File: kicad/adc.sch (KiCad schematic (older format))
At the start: 18 parts, among them U1 SIT1602BI-21-XXE-8.192000G

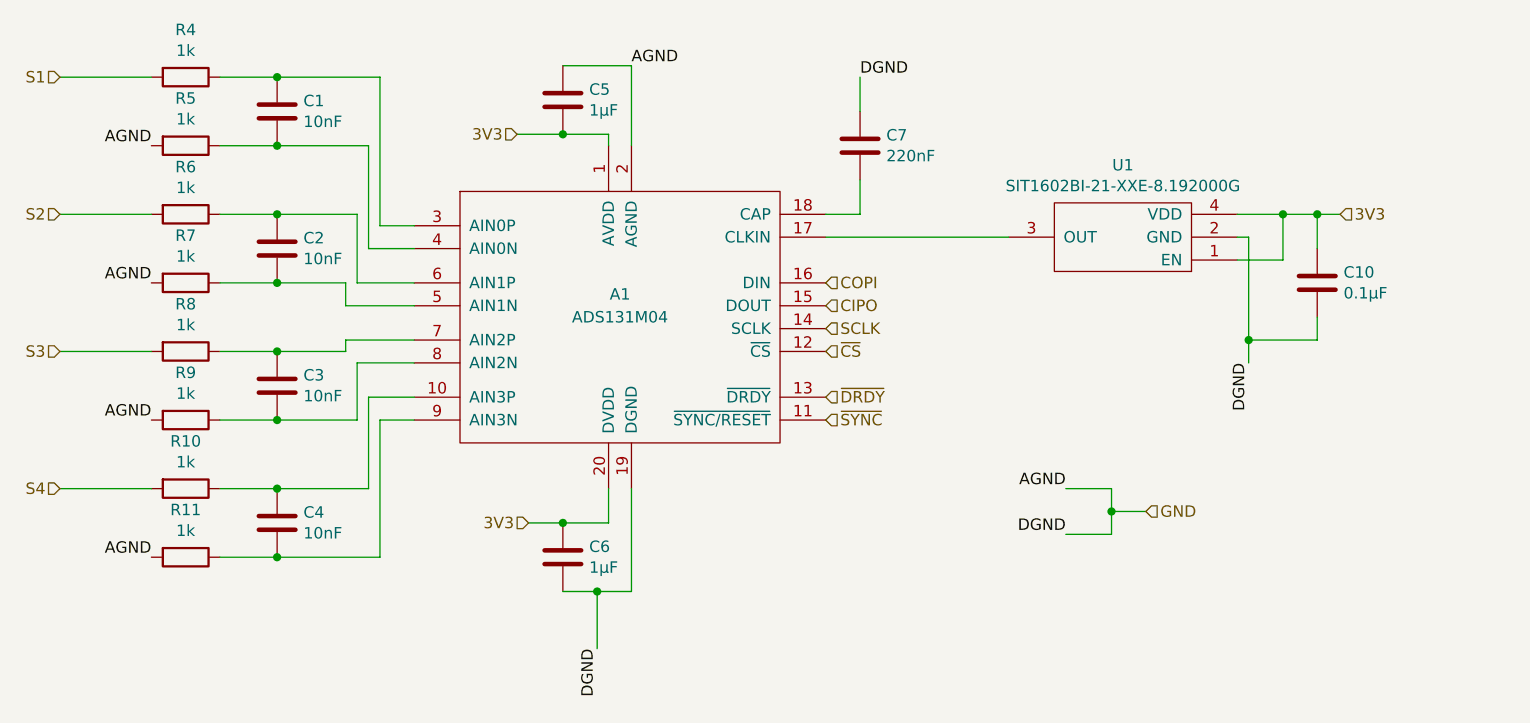
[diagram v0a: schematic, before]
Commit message: switch clock and add bypass
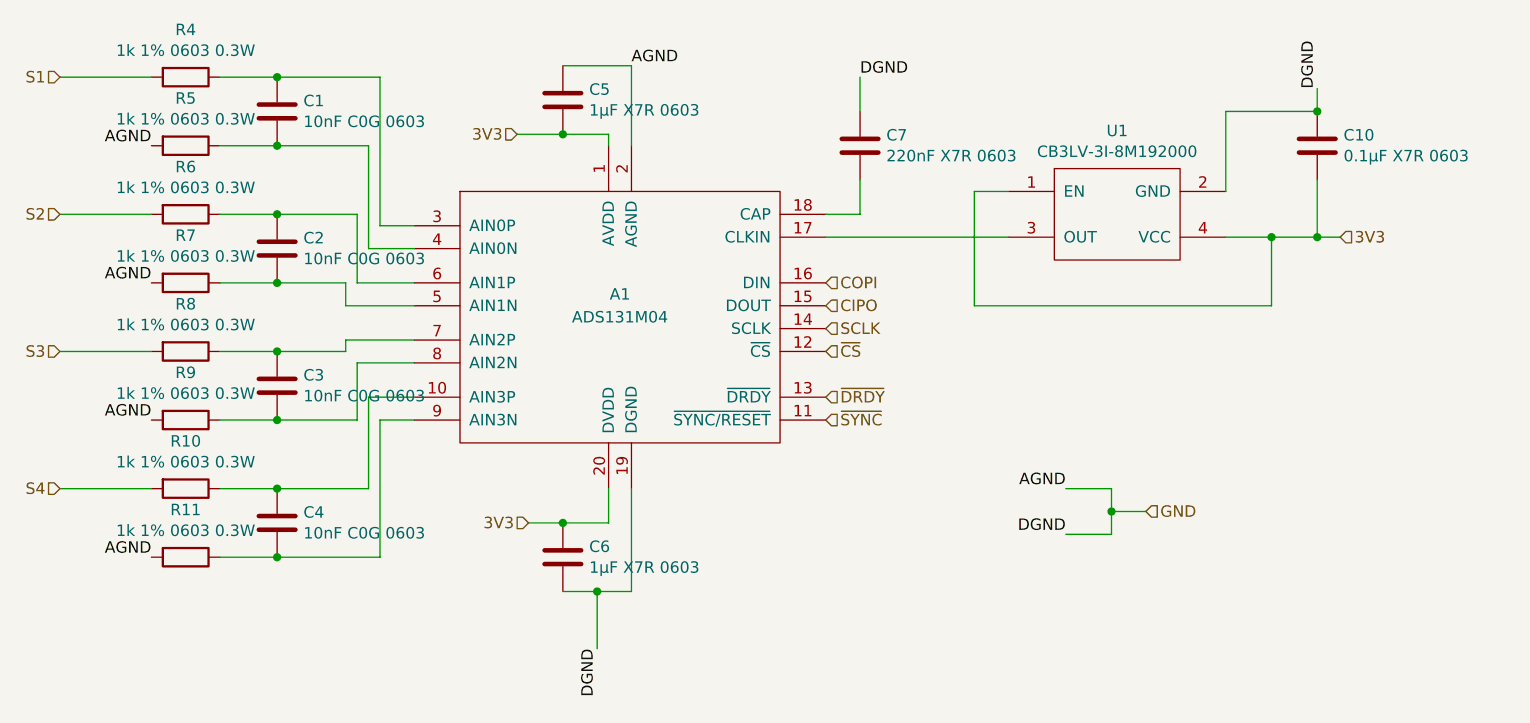
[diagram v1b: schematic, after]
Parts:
- removed U1: SIT1602BI-21-XXE-8.192000G, HH_SiTime:SIT1602BI-21-XXE-8.192000G, symbol HH_SiTime:SIT1602BI-21-XXE-8.192000G
- added U1: CB3LV-3I-8M192000, HH_CTS-FrequencyControls:CB3LV-3I-8M192000, symbol HH_CTS-FrequencyControls:CB3LV-3I-8M192000
- C1, C2, C3, C4: value 10nF -> 10nF C0G 0603
- C10: value 0.1µF -> 0.1µF X7R 0603
- C5, C6: value 1µF -> 1µF X7R 0603
- C7: value 220nF -> 220nF X7R 0603
- R10, R11, R4, R5, R6, R7, R8, R9: value 1k -> 1k 1% 0603 0.3W
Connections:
- net 3V3: now also C10.2, U1.1 (EN), U1.4 (VCC); no longer C10.1
- net GND: now also C10.1, U1.2 (GND); no longer C10.2
- net at A1.17 (CLKIN): now also U1.3 (OUT)
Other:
- moved on the sheet: C10
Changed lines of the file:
@@
 	1    0    0    -1
 $EndComp
-$Comp
-L HH_SiTime:SIT1602BI-21-XXE-8.192000G U?
-U 1 1 5FC7855A
-P 7850 3450
-AR Path="/5FC7855A" Ref="U?"  Part="1"
-AR Path="/5FC723A8/5FC7855A" Ref="U1"  Part="1"
-F 0 "U1" H 7850 3135 50  0000 C CNN
-F 1 "SIT1602BI-21-XXE-8.192000G" H 7850 3226 50  0000 C CNN
-F 2 "HH_SiTime:SIT1602BI-21-XXE-8.192000G" H 7850 3450 50  0001 C CNN
-F 3 "https://www.sitime.com/datasheet/SiT1602" H 7850 3450 50  0001 C CNN
-F 4 "1473-SIT1602BI-21-XXE-8.192000G-ND" H 7850 3450 50  0001 C CNN "Digi-Key Part Number"
-F 5 "SiTime" H 7850 3450 50  0001 C CNN "Manufacturer"
-F 6 "SIT1602BI-21-XXE-8.192000G" H 7850 3450 50  0001 C CNN "Manufacturer Part Number"
-F 7 "MEMS OSC XO 8.1920MHZ H/LV-CMOS" H 7850 3450 50  0001 C CNN "Description"
-	1    7850 3450
-	-1   0    0    1
-$EndComp
-Wire Wire Line
-	8800 3350 8700 3350
-Wire Wire Line
-	8550 3350 8550 3550
-Wire Wire Line
-	8550 3550 8350 3550
-Connection ~ 8550 3350
-Wire Wire Line
-	8550 3350 8350 3350
-Wire Wire Line
-	8400 3450 8350 3450
 Wire Wire Line
 	5600 4700 5600 4550
@@
 AR Path="/5FC723A8/5FC78580" Ref="C5"  Part="1"
 F 0 "C5" H 5515 2896 50  0000 L CNN
-F 1 "1µF" H 5515 2805 50  0000 L CNN
+F 1 "1µF X7R 0603" H 5515 2805 50  0000 L CNN
 F 2 "Capacitor_SMD:C_0603_1608Metric" H 5438 2700 50  0001 C CNN
 F 3 "~" H 5400 2850 50  0001 C CNN
@@
 AR Path="/5FC723A8/5FC78590" Ref="C6"  Part="1"
 F 0 "C6" H 5515 4896 50  0000 L CNN
-F 1 "1µF" H 5515 4805 50  0000 L CNN
+F 1 "1µF X7R 0603" H 5515 4805 50  0000 L CNN
 F 2 "Capacitor_SMD:C_0603_1608Metric" H 5438 4700 50  0001 C CNN
 F 3 "~" H 5400 4850 50  0001 C CNN
@@
 AR Path="/5FC723A8/5FC7859D" Ref="C7"  Part="1"
 F 0 "C7" H 6815 3096 50  0000 L CNN
-F 1 "220nF" H 6815 3005 50  0000 L CNN
+F 1 "220nF X7R 0603" H 6815 3005 50  0000 L CNN
 F 2 "Capacitor_SMD:C_0603_1608Metric" H 6738 2900 50  0001 C CNN
 F 3 "~" H 6700 3050 50  0001 C CNN
@@
 Wire Wire Line
 	6550 3450 7350 3450
-Text HLabel 8800 3350 2    50   Input ~ 0
+Text HLabel 8800 3450 2    50   Input ~ 0
 3V3
 Text HLabel 5250 4700 0    50   Input ~ 0
@@
 P 4150 2900
 F 0 "C1" H 4265 2946 50  0000 L CNN
-F 1 "10nF" H 4265 2855 50  0000 L CNN
+F 1 "10nF C0G 0603" H 4265 2855 50  0000 L CNN
 F 2 "Capacitor_SMD:C_0603_1608Metric" H 4188 2750 50  0001 C CNN
 F 3 "~" H 4150 2900 50  0001 C CNN
@@
 P 3750 2750
 F 0 "R4" V 3543 2750 50  0000 C CNN
-F 1 "1k" V 3634 2750 50  0000 C CNN
+F 1 "1k 1% 0603 0.3W" V 3634 2750 50  0000 C CNN
 F 2 "Resistor_SMD:R_0603_1608Metric" V 3680 2750 50  0001 C CNN
 F 3 "~" H 3750 2750 50  0001 C CNN
@@
 P 3750 3050
 F 0 "R5" V 3543 3050 50  0000 C CNN
-F 1 "1k" V 3634 3050 50  0000 C CNN
+F 1 "1k 1% 0603 0.3W" V 3634 3050 50  0000 C CNN
 F 2 "Resistor_SMD:R_0603_1608Metric" V 3680 3050 50  0001 C CNN
 F 3 "~" H 3750 3050 50  0001 C CNN
@@
 P 4150 3500
 F 0 "C2" H 4265 3546 50  0000 L CNN
-F 1 "10nF" H 4265 3455 50  0000 L CNN
+F 1 "10nF C0G 0603" H 4265 3455 50  0000 L CNN
 F 2 "Capacitor_SMD:C_0603_1608Metric" H 4188 3350 50  0001 C CNN
 F 3 "~" H 4150 3500 50  0001 C CNN
@@
 P 3750 3350
 F 0 "R6" V 3543 3350 50  0000 C CNN
-F 1 "1k" V 3634 3350 50  0000 C CNN
+F 1 "1k 1% 0603 0.3W" V 3634 3350 50  0000 C CNN
 F 2 "Resistor_SMD:R_0603_1608Metric" V 3680 3350 50  0001 C CNN
 F 3 "~" H 3750 3350 50  0001 C CNN
@@
 P 3750 3650
 F 0 "R7" V 3543 3650 50  0000 C CNN
-F 1 "1k" V 3634 3650 50  0000 C CNN
+F 1 "1k 1% 0603 0.3W" V 3634 3650 50  0000 C CNN
 F 2 "Resistor_SMD:R_0603_1608Metric" V 3680 3650 50  0001 C CNN
 F 3 "~" H 3750 3650 50  0001 C CNN
@@
 P 4150 4100
 F 0 "C3" H 4265 4146 50  0000 L CNN
-F 1 "10nF" H 4265 4055 50  0000 L CNN
+F 1 "10nF C0G 0603" H 4265 4055 50  0000 L CNN
 F 2 "Capacitor_SMD:C_0603_1608Metric" H 4188 3950 50  0001 C CNN
 F 3 "~" H 4150 4100 50  0001 C CNN
@@
 P 3750 3950
 F 0 "R8" V 3543 3950 50  0000 C CNN
-F 1 "1k" V 3634 3950 50  0000 C CNN
+F 1 "1k 1% 0603 0.3W" V 3634 3950 50  0000 C CNN
 F 2 "Resistor_SMD:R_0603_1608Metric" V 3680 3950 50  0001 C CNN
 F 3 "~" H 3750 3950 50  0001 C CNN
@@
 P 3750 4250
 F 0 "R9" V 3543 4250 50  0000 C CNN
-F 1 "1k" V 3634 4250 50  0000 C CNN
+F 1 "1k 1% 0603 0.3W" V 3634 4250 50  0000 C CNN
 F 2 "Resistor_SMD:R_0603_1608Metric" V 3680 4250 50  0001 C CNN
 F 3 "~" H 3750 4250 50  0001 C CNN
@@
 P 4150 4700
 F 0 "C4" H 4265 4746 50  0000 L CNN
-F 1 "10nF" H 4265 4655 50  0000 L CNN
+F 1 "10nF C0G 0603" H 4265 4655 50  0000 L CNN
 F 2 "Capacitor_SMD:C_0603_1608Metric" H 4188 4550 50  0001 C CNN
 F 3 "~" H 4150 4700 50  0001 C CNN
@@
 P 3750 4550
 F 0 "R10" V 3543 4550 50  0000 C CNN
-F 1 "1k" V 3634 4550 50  0000 C CNN
+F 1 "1k 1% 0603 0.3W" V 3634 4550 50  0000 C CNN
 F 2 "Resistor_SMD:R_0603_1608Metric" V 3680 4550 50  0001 C CNN
 F 3 "~" H 3750 4550 50  0001 C CNN
@@
 P 3750 4850
 F 0 "R11" V 3543 4850 50  0000 C CNN
-F 1 "1k" V 3634 4850 50  0000 C CNN
+F 1 "1k 1% 0603 0.3W" V 3634 4850 50  0000 C CNN
 F 2 "Resistor_SMD:R_0603_1608Metric" V 3680 4850 50  0001 C CNN
 F 3 "~" H 3750 4850 50  0001 C CNN
@@
 Text Label 5550 5250 3    50   ~ 0
 DGND
-Text Label 8400 4000 3    50   ~ 0
+Text Label 8700 2800 1    50   ~ 0
 DGND
 Text Label 7600 4550 2    50   ~ 0
@@
 L Device:C C10
 U 1 1 5FCED712
-P 8700 3650
-F 0 "C10" H 8815 3696 50  0000 L CNN
-F 1 "0.1µF" H 8815 3605 50  0000 L CNN
-F 2 "Capacitor_SMD:C_0603_1608Metric" H 8738 3500 50  0001 C CNN
-F 3 "~" H 8700 3650 50  0001 C CNN
-	1    8700 3650
-	1    0    0    -1
-$EndComp
-Wire Wire Line
-	8700 3500 8700 3350
-Connection ~ 8700 3350
-Wire Wire Line
-	8700 3350 8550 3350
-Wire Wire Line
-	8400 3450 8400 3900
-Wire Wire Line
-	8400 3900 8700 3900
-Wire Wire Line
-	8700 3900 8700 3800
-Connection ~ 8400 3900
-Wire Wire Line
-	8400 3900 8400 4000
+P 8700 3050
+F 0 "C10" H 8815 3096 50  0000 L CNN
+F 1 "0.1µF X7R 0603" H 8815 3005 50  0000 L CNN
+F 2 "Capacitor_SMD:C_0603_1608Metric" H 8738 2900 50  0001 C CNN
+F 3 "~" H 8700 3050 50  0001 C CNN
+	1    8700 3050
+	1    0    0    -1
+$EndComp
+$Comp
+L HH_CTS-FrequencyControls:CB3LV-3I-8M192000 U1
+U 1 1 5FCD2FA9
+P 7800 3350
+F 0 "U1" H 7825 3715 50  0000 C CNN
+F 1 "CB3LV-3I-8M192000" H 7825 3624 50  0000 C CNN
+F 2 "HH_CTS-FrequencyControls:CB3LV-3I-8M192000" H 7800 3350 50  0001 C CNN
+F 3 "https://www.ctscorp.com/wp-content/uploads/2015/11/008-0256-0.pdf" H 7800 3350 50  0001 C CNN
+F 4 "110-CB3LV-3I-8M192000CT-ND" H 7800 3350 50  0001 C CNN "Digi-Key Part Number"
+F 5 "CTS-Frequency Controls" H 7800 3350 50  0001 C CNN "Manufacturer"
+F 6 "CB3LV-3I-8M192000" H 7800 3350 50  0001 C CNN "Manufacturer Part Number"
+F 7 "XTAL OSC XO 8.1920MHZ HCMOS TTL" H 7800 3350 50  0001 C CNN "Description"
+	1    7800 3350
+	1    0    0    -1
+$EndComp
+Wire Wire Line
+	8700 3450 8700 3200
+Connection ~ 8700 3450
+Wire Wire Line
+	8700 3450 8800 3450
+Wire Wire Line
+	8300 3250 8300 2900
+Wire Wire Line
+	8300 2900 8700 2900
+Wire Wire Line
+	8700 2900 8700 2800
+Connection ~ 8700 2900
+Wire Wire Line
+	8300 3450 8500 3450
+Wire Wire Line
+	8500 3450 8500 3750
+Wire Wire Line
+	8500 3750 7200 3750
+Wire Wire Line
+	7200 3750 7200 3250
+Wire Wire Line
+	7200 3250 7350 3250
+Connection ~ 8500 3450
+Wire Wire Line
+	8500 3450 8700 3450
 $EndSCHEMATC
